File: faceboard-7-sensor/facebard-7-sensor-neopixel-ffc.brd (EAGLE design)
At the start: 27 x 93.4 mm, 33 parts, among them J1 686114148922, J2 686114148922, Q1 QRE1113, Q2 QRE1113, Q3 QRE1113, Q4 QRE1113, Q5 QRE1113, Q6 QRE1113, Q7 QRE1113, U1 CD4051BE

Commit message: add ffc
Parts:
- removed J2: 686114148922, 686114148922:686114148922
- added FFCIN, FFCOUT: 52806-1410, 52806-1410:528061410
- added J3: 1-1734592-4, 1-1734592-4:CONN_1-1734592-4_TYCO
- added SJ1, SJ2, SJ3, SJ4, SJ5, SJ6, SJ7: (no value), jumper:SJ
- J1: value 686114148922 -> 1-1734592-4; device 686114148922:686114148922 -> 1-1734592-4:CONN_1-1734592-4_TYCO
- moved J1 8.14 mm to (18.0, 86.0), turned to 0 degrees
- moved D1 2.08 mm to (25.9, 2.61)
- moved D2 2.08 mm to (25.9, 16.6)
- moved D3 2.08 mm to (25.9, 30.6)
- moved D4 2.08 mm to (25.9, 44.7)
- moved D5 2.08 mm to (25.9, 58.7)
- moved D6 2.08 mm to (25.9, 72.7)
- moved D7 2.08 mm to (25.9, 86.7)
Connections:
- net 3V: now also FFCIN.2, FFCOUT.13, J1.2, J3.13; no longer J1.13, J2.2
- net 5V: now also FFCIN.3, FFCOUT.12, J1.3, J3.12; no longer J1.12, J2.3
- net A: now also FFCIN.4, FFCOUT.11, J1.4, J3.11; no longer J1.11, J2.4
- net B: now also FFCIN.5, FFCOUT.10, J1.5, J3.10; no longer J1.10, J2.5
- net C: now also FFCIN.6, FFCOUT.9, J1.6, J3.9; no longer J1.9, J2.6
- net GND: now also FFCIN.1, FFCOUT.14, J1.1, J3.14; no longer J1.14, J1.MP1, J1.MP2, J2.1, J2.MP1, J2.MP2
- net LEDDIN: now also FFCIN.7, J1.7; no longer J2.7
- net LEDDOUT: now also FFCOUT.8, J3.8; no longer J1.8
- net N$18: no longer D3.4
- net SIG: now also SJ1.2, SJ2.2, SJ3.2, SJ4.2, SJ5.2, SJ6.2, SJ7.2
- net SIG1: now also FFCIN.8, FFCOUT.7, J1.14, J3.1, SJ1.1; no longer J1.1, J2.14
- net SIG2: now also FFCIN.9, FFCOUT.6, J1.13, J3.2, SJ2.1; no longer J1.2, J2.13
- net SIG3: now also FFCIN.10, FFCOUT.5, J1.12, J3.3, SJ3.1; no longer J1.3, J2.12
- net SIG4: now also FFCIN.11, FFCOUT.4, J1.11, J3.4, SJ4.1; no longer J1.4, J2.11
- net SIG5: now also FFCIN.12, FFCOUT.3, J1.10, J3.5, SJ5.1; no longer J1.5, J2.10
- net SIG6: now also FFCIN.13, FFCOUT.2, J1.9, J3.6, SJ6.1; no longer J1.6, J2.9
- net SIG7: now also FFCIN.14, FFCOUT.1, J1.8, J3.7, SJ7.1; no longer J1.7, J2.8
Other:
- board size 27 x 93.4 mm -> 29 x 93.4 mm

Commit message: remove 0.5mm ffc
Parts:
- removed J1, J3: 1-1734592-4, 1-1734592-4:CONN_1-1734592-4_TYCO
- removed SV1, SV4: (no value), con-lstb:MA07-1
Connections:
- net 3V: no longer J1.2, J3.13
- net 5V: no longer J1.3, J3.12
- net A: no longer J1.4, J3.11
- net B: no longer J1.5, J3.10
- net C: no longer J1.6, J3.9
- net GND: no longer J1.1, J3.14
- net LEDDIN: no longer J1.7
- net LEDDOUT: no longer J3.8
- net N$18: now also D3.4
- net SIG: no longer SV1.1, SV1.2, SV1.3, SV1.4, SV1.5, SV1.6, SV1.7
- net SIG1: no longer J1.14, J3.1, SV4.1
- net SIG2: no longer J1.13, J3.2, SV4.2
- net SIG3: no longer J1.12, J3.3, SV4.3
- net SIG4: no longer J1.11, J3.4, SV4.4
- net SIG5: no longer J1.10, J3.5, SV4.5
- net SIG6: no longer J1.9, J3.6, SV4.6
- net SIG7: no longer J1.8, J3.7, SV4.7

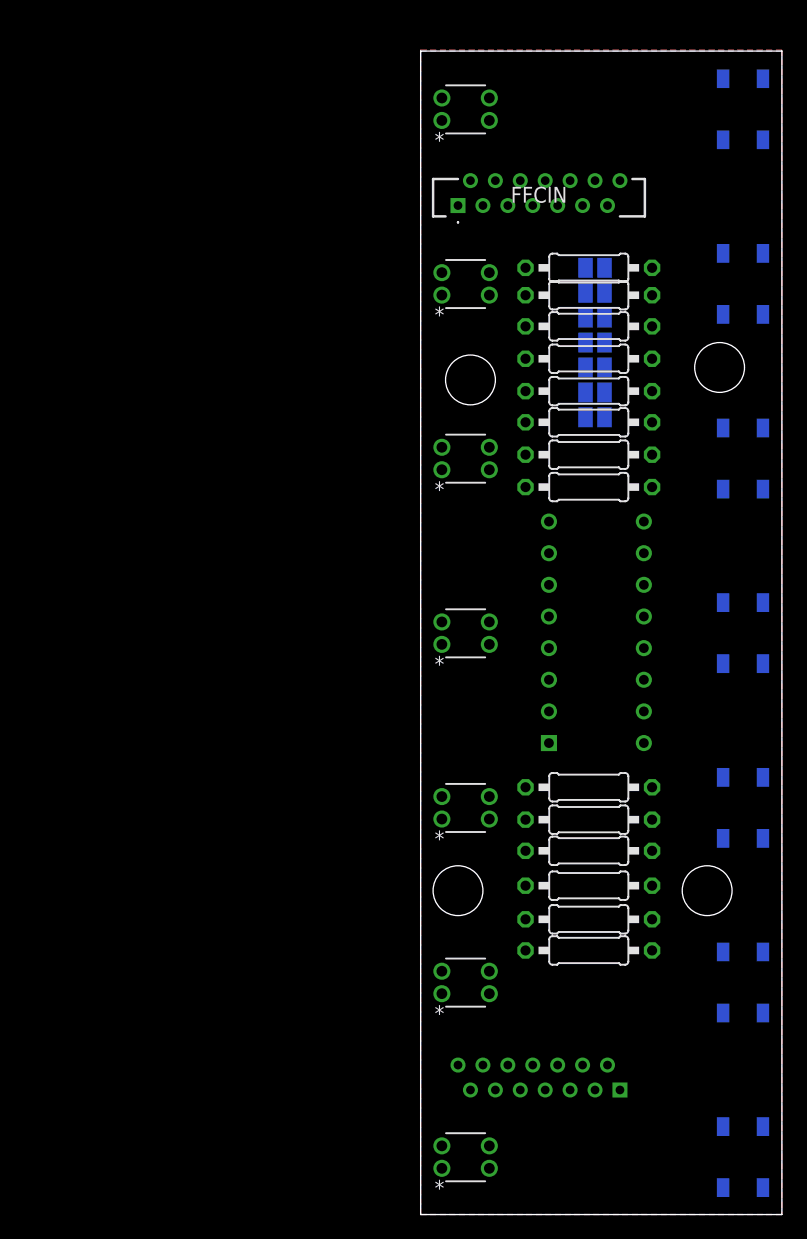
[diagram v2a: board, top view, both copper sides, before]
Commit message: add ffc boards
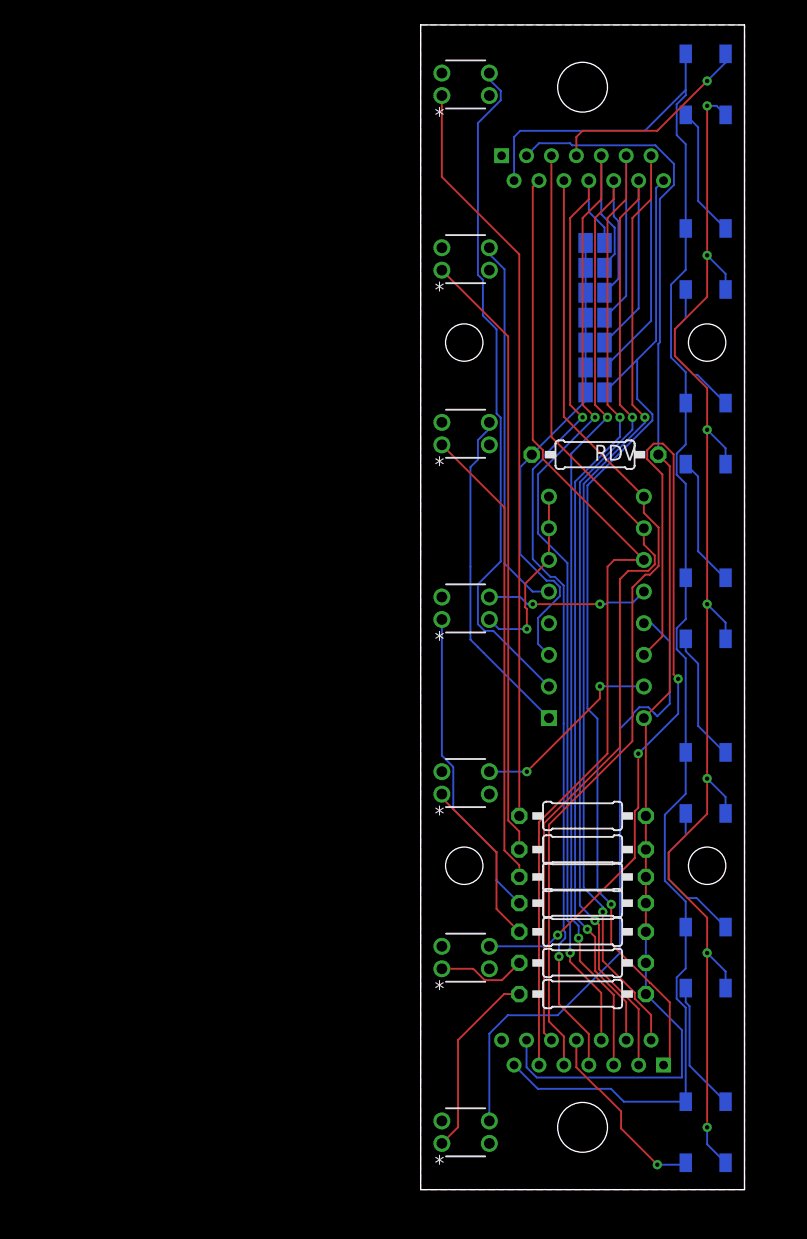
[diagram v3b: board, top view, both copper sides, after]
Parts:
- removed R10, R12, R14, R2, R4, R6, R8: 100k, rcl:0207/10
- added RDV: 1M, rcl:0207/10
- moved FFCOUT 75.6 mm to (6.50, 83.0), turned to 180 degrees
- moved FFCIN 70.9 mm to (19.5, 10.0), flipped to the bottom
- moved R13 44.0 mm to (13.0, 30.0)
- moved R11 42.0 mm to (13.0, 27.3)
- moved R9 39.0 mm to (13.0, 25.1)
- moved R7 36.0 mm to (13.0, 23.0)
- moved R3 9.01 mm to (13.0, 18.2)
- moved R5 9.01 mm to (13.0, 20.7)
- moved R1 6.02 mm to (13.0, 15.7)
- moved D1 3.61 mm to (22.9, 4.61)
- moved D2 3.61 mm to (22.9, 18.6)
- moved D3 3.61 mm to (22.9, 32.6)
- moved D4 3.61 mm to (22.9, 46.7)
- moved D5 3.61 mm to (22.9, 60.7)
- moved D6 3.61 mm to (22.9, 74.7)
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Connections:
- net 3V: now also FFCIN.13, FFCOUT.2; no longer FFCIN.2, FFCOUT.13
- net 5V: now also FFCIN.12, FFCOUT.3, RDV.2; no longer FFCIN.3, FFCOUT.12, R10.2, R12.2, R14.2, R2.2, R4.2, R6.2, R8.2
- net A: now also FFCIN.11, FFCOUT.4; no longer FFCIN.4, FFCOUT.11
- net B: now also FFCIN.10, FFCOUT.5; no longer FFCIN.5, FFCOUT.10
- net C: now also FFCIN.9, FFCOUT.6; no longer FFCIN.6, FFCOUT.9
- net GND: now also FFCIN.14, FFCOUT.1; no longer FFCIN.1, FFCOUT.14
- net LEDDIN: now also FFCIN.8; no longer FFCIN.7
- net LEDDOUT: now also FFCOUT.7; no longer FFCOUT.8
- net Q1SIG: no longer R2.1
- net Q2SIG: no longer R4.1
- net Q3SIG: no longer R6.1
- net Q4SIG: no longer R8.1
- net Q5SIG: no longer R10.1
- net Q6SIG: no longer R12.1
- net Q7SIG: no longer R14.1
- net SIG: now also RDV.1
- net SIG1: now also FFCIN.7, FFCOUT.8; no longer FFCIN.8, FFCOUT.7
- net SIG2: now also FFCIN.6, FFCOUT.9; no longer FFCIN.9, FFCOUT.6
- net SIG3: now also FFCIN.5, FFCOUT.10; no longer FFCIN.10, FFCOUT.5
- net SIG4: now also FFCIN.4, FFCOUT.11; no longer FFCIN.11, FFCOUT.4
- net SIG5: now also FFCIN.3, FFCOUT.12; no longer FFCIN.12, FFCOUT.3
- net SIG6: now also FFCIN.2, FFCOUT.13; no longer FFCIN.13, FFCOUT.2
- net SIG7: now also FFCIN.1, FFCOUT.14; no longer FFCIN.14, FFCOUT.1
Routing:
- net GND: track 0.00 -> 123.7 mm, vias 0 -> 8
- net 3V: track 0.00 -> 122.7 mm
- net 5V: track 0.00 -> 104.3 mm
- net SIG6: track 0.00 -> 94.9 mm, vias 0 -> 2
- net SIG5: track 0.00 -> 89.9 mm, vias 0 -> 2
- net SIG4: track 0.00 -> 88.9 mm, vias 0 -> 2
- net SIG2: track 0.00 -> 85.8 mm, vias 0 -> 2
- net SIG3: track 0.00 -> 84.3 mm, vias 0 -> 2
- net SIG1: track 0.00 -> 81.7 mm, vias 0 -> 2
- net SIG7: track 0.00 -> 81.2 mm, vias 0 -> 1
- net A: track 0.00 -> 79.8 mm
- net B: track 0.00 -> 79.4 mm
- net C: track 0.00 -> 78.5 mm
- net Q2SIG: track 0.00 -> 68.9 mm, vias 0 -> 3
- net N$13: track 0.00 -> 60.4 mm
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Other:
- board size 29 x 93.4 mm -> 26 x 93.5 mm
- board text added: "1"
- board text added: "2"
- board text added: "3"
- board text added: "4"
- board text added: "5"
- board text added: "6"
- board text added: "7"
- board text added: "NEMUS Face Board v0.1.1"
- board text removed: "3V"
- board text removed: "5V"
- board text removed: "A"
- board text removed: "C"
- board text removed: "DI"
- board text removed: "DO"
- board text removed: "GND"
- board text removed: "INT"
- board text removed: "NEMUS Face Board v0.1.0"
- board text removed: "SIG"

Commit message: tidy routing
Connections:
- net Q1SIG renamed C0
- net Q2SIG renamed C1
- net Q3SIG renamed C2
- net Q4SIG renamed C3
- net Q5SIG renamed C4
- net Q6SIG renamed C5
- net Q7SIG renamed C6
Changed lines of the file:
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@@
 <wire x1="6.7" y1="15.7" x2="7.92" y2="15.7" width="0.1524" layer="1"/>
 </signal>
-<signal name="Q1SIG">
+<signal name="C0">
 <contactref element="U1" pad="13"/>
-<contactref element="Q1" pad="3"/>
-<wire x1="5.515" y1="5.5134" x2="5.515" y2="12.515" width="0.1524" layer="16"/>
 <wire x1="5.515" y1="12.515" x2="7" y2="14" width="0.1524" layer="16"/>
 <wire x1="7" y1="14" x2="11" y2="14" width="0.1524" layer="16"/>
@@
 <wire x1="20" y1="39" x2="20" y2="44" width="0.1524" layer="16"/>
 <wire x1="20" y1="44" x2="18.53" y2="45.47" width="0.1524" layer="16"/>
+<contactref element="Q1" pad="3"/>
+<wire x1="5.515" y1="5.5134" x2="5.515" y2="12.515" width="0.1524" layer="16"/>
 </signal>
 <signal name="GND">
@@
 <wire x1="6.5356" y1="16.8156" x2="7.92" y2="18.2" width="0.1524" layer="1"/>
 </signal>
-<signal name="Q2SIG">
-<contactref element="Q2" pad="3"/>
+<signal name="C1">
 <contactref element="U1" pad="14"/>
 <via x="11" y="20.4334" extent="1-16" drill="0.35"/>
@@
 <wire x1="20.3048" y1="41.3684" x2="20.3048" y2="59.0324375" width="0.1524" layer="1"/>
 <wire x1="20.3048" y1="59.0324375" x2="19.4482375" y2="59.889" width="0.1524" layer="1"/>
+<wire x1="10.1" y1="19.5334" x2="11" y2="20.4334" width="0.1524" layer="16"/>
+<contactref element="Q2" pad="3"/>
 <wire x1="5.515" y1="19.5334" x2="10.1" y2="19.5334" width="0.1524" layer="16"/>
-<wire x1="10.1" y1="19.5334" x2="11" y2="20.4334" width="0.1524" layer="16"/>
 </signal>
 <signal name="N$5">
@@
 <wire x1="6.0922" y1="27.073725" x2="1.705" y2="31.460925" width="0.1524" layer="1"/>
 </signal>
-<signal name="Q3SIG">
-<contactref element="Q3" pad="3"/>
+<signal name="C2">
 <contactref element="U1" pad="15"/>
-<wire x1="5.515" y1="33.5534" x2="8.5268" y2="33.5534" width="0.1524" layer="16"/>
 <via x="8.5268" y="33.5534" extent="1-16" drill="0.35"/>
 <wire x1="8.5268" y1="33.5534" x2="14.3932" y2="39.4198" width="0.1524" layer="1"/>
@@
 <wire x1="14.3932" y1="40.4" x2="17.91" y2="40.4" width="0.1524" layer="16"/>
 <wire x1="17.91" y1="40.4" x2="17.92" y2="40.39" width="0.1524" layer="16"/>
+<contactref element="Q3" pad="3"/>
+<wire x1="5.515" y1="33.5534" x2="8.5268" y2="33.5534" width="0.1524" layer="16"/>
 </signal>
 <signal name="N$7">
@@
 <wire x1="2.6194" y1="30.546525" x2="2.6194" y2="33.9321625" width="0.1524" layer="16"/>
 </signal>
-<signal name="Q4SIG">
-<contactref element="Q4" pad="3"/>
+<signal name="C3">
 <contactref element="U1" pad="12"/>
-<wire x1="5.515" y1="47.5734" x2="8" y2="47.5734" width="0.1524" layer="16"/>
 <wire x1="15" y1="47.1337" x2="17.0437" y2="47.1337" width="0.1524" layer="16"/>
 <wire x1="17.0437" y1="47.1337" x2="17.92" y2="48.01" width="0.1524" layer="16"/>
-<wire x1="8" y1="47.5734" x2="8.5734" y2="47" width="0.1524" layer="16"/>
+<wire x1="8.0267" y1="47.5467" x2="8.5734" y2="47" width="0.1524" layer="16"/>
 <wire x1="8.5734" y1="47" x2="9" y2="47" width="0.1524" layer="16"/>
 <via x="9" y="47" extent="1-16" drill="0.35"/>
@@
 <wire x1="15" y1="47.1337" x2="14.8663" y2="47" width="0.1524" layer="16"/>
 <wire x1="9" y1="47" x2="14.3932" y2="47" width="0.1524" layer="1"/>
+<contactref element="Q4" pad="3"/>
+<wire x1="5.515" y1="47.5734" x2="8" y2="47.5734" width="0.1524" layer="16"/>
+<wire x1="8" y1="47.5734" x2="8.0267" y2="47.5467" width="0.1524" layer="16"/>
 </signal>
 <signal name="N$9">
@@
 <wire x1="6.7262" y1="27.2365625" x2="6.7262" y2="54.7688" width="0.1524" layer="1"/>
 </signal>
-<signal name="Q5SIG">
-<contactref element="Q5" pad="3"/>
+<signal name="C4">
 <contactref element="U1" pad="1"/>
-<wire x1="4.6006" y1="43.5494" x2="5.075" y2="43.075" width="0.1524" layer="16"/>
-<wire x1="5.075" y1="43.075" x2="10.3" y2="37.85" width="0.1524" layer="16"/>
-<wire x1="5.515" y1="61.5934" x2="5.515" y2="61.0831625" width="0.1524" layer="16"/>
+<wire x1="4" y1="44.15" x2="10.3" y2="37.85" width="0.1524" layer="16"/>
 <wire x1="4.6006" y1="58.6006" x2="4" y2="58" width="0.1524" layer="16"/>
 <wire x1="5.515" y1="61.0831625" x2="4.6006" y2="60.1687625" width="0.1524" layer="16"/>
 <wire x1="4.6006" y1="60.1687625" x2="4.6006" y2="58.6006" width="0.1524" layer="16"/>
-<wire x1="4" y1="58" x2="4" y2="50" width="0.1524" layer="16"/>
-<wire x1="4" y1="50" x2="4" y2="44.15" width="0.1524" layer="16"/>
-<wire x1="4" y1="44.15" x2="4.6006" y2="43.5494" width="0.1524" layer="16"/>
+<wire x1="4" y1="58" x2="4" y2="44.15" width="0.1524" layer="16"/>
+<contactref element="Q5" pad="3"/>
+<wire x1="5.515" y1="61.5934" x2="5.515" y2="61.0831625" width="0.1524" layer="16"/>
 </signal>
 <signal name="N$11">
@@
 <wire x1="7.031" y1="29.6317625" x2="7.031" y2="68.484" width="0.1524" layer="1"/>
 </signal>
-<signal name="Q6SIG">
-<contactref element="Q6" pad="3"/>
+<signal name="C5">
 <contactref element="U1" pad="5"/>
-<wire x1="5.515" y1="75.6134" x2="5.515" y2="75.1031625" width="0.1524" layer="16"/>
 <wire x1="5.515" y1="75.1031625" x2="6.7342" y2="73.8839625" width="0.1524" layer="16"/>
 <wire x1="6.7342" y1="73.8839625" x2="6.7342" y2="50.2658" width="0.1524" layer="16"/>
 <wire x1="8.99" y1="48.01" x2="10.3" y2="48.01" width="0.1524" layer="16"/>
 <wire x1="6.7342" y1="50.2658" x2="8.99" y2="48.01" width="0.1524" layer="16"/>
+<contactref element="Q6" pad="3"/>
+<wire x1="5.515" y1="75.6134" x2="5.515" y2="75.1031625" width="0.1524" layer="16"/>
 </signal>
 <signal name="N$13">
@@
 <wire x1="7.92" y1="75.08" x2="1.705" y2="81.295" width="0.1524" layer="1"/>
 </signal>
-<signal name="Q7SIG">
-<contactref element="Q7" pad="3"/>
+<signal name="C6">
 <contactref element="U1" pad="2"/>
 <wire x1="6.4294" y1="88.2087625" x2="6.4294" y2="87.4512375" width="0.1524" layer="16"/>
-<wire x1="5.515" y1="89.6334" x2="5.515" y2="89.1231625" width="0.1524" layer="16"/>
 <wire x1="5.515" y1="89.1231625" x2="6.4294" y2="88.2087625" width="0.1524" layer="16"/>
 <wire x1="4.6006" y1="73.4312375" x2="5" y2="73.0318375" width="0.1524" layer="16"/>
@@
 <wire x1="4.6006" y1="48.6006" x2="4.6006" y2="45.3912375" width="0.1524" layer="16"/>
 <wire x1="6.4294" y1="50.4294" x2="4.6006" y2="48.6006" width="0.1524" layer="16"/>
+<contactref element="Q7" pad="3"/>
+<wire x1="5.515" y1="89.6334" x2="5.515" y2="89.1231625" width="0.1524" layer="16"/>
 </signal>
 <signal name="SIG">

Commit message: change divide resistor value
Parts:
- RDV: value 1M -> 100k
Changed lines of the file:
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@@
 <attribute name="VALUE" x="13.5999" y="64" size="0.02" layer="28" rot="MR0"/>
 </element>
-<element name="RDV" library="rcl" library_urn="urn:adsk.eagle:library:334" package="0207/10" package3d_urn="urn:adsk.eagle:package:23491/2" value="1M" x="14" y="59" smashed="yes">
+<element name="RDV" library="rcl" library_urn="urn:adsk.eagle:library:334" package="0207/10" package3d_urn="urn:adsk.eagle:package:23491/2" value="100k" x="14" y="59" smashed="yes">
 <attribute name="NAME" x="13.952" y="58.524" size="1.27" layer="25" ratio="10"/>
 <attribute name="POPULARITY" value="81" x="14" y="59" size="1.778" layer="27" display="off"/>

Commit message: re-draw schematics
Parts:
- moved U1 44.4 mm to (-31.1, 21.9), flipped to the top, turned to 0 degrees
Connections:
- net LEDDIN renamed DIN
- net LEDDOUT renamed DOUT
- net SIG1 renamed S1
- net SIG2 renamed S2
- net SIG3 renamed S3
- net SIG4 renamed S4
- net SIG5 renamed S5
- net SIG6 renamed S6
- net SIG7 renamed S7
- removed net 5V: FFCIN.12, FFCOUT.3, R1.1, R11.1, R13.1, R3.1, R5.1, R7.1, R9.1, RDV.2, U1.16
- removed net N$9: Q5.1, R9.2
- new net N$2: FFCOUT.3, R1.1, R11.1, R13.1, R3.1, R5.1, R7.1, R9.1
- new net VCC: FFCIN.12, RDV.2, U1.16
- net GND: no longer FFCIN.14
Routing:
- net 5V: track 104.3 -> 0.00 mm
- net VCC: track 0.00 -> 38.2 mm
- net N$9: track 37.3 -> 0.00 mm
- net GND: track 123.7 -> 108.9 mm, vias 8 -> 7
- net A: track 79.8 -> 65.9 mm
- net C: track 78.5 -> 68.1 mm
- net C4: track 27.0 -> 18.1 mm
- net C6: track 54.7 -> 48.3 mm
- net S3: track 84.3 -> 78.6 mm
- net S6: track 94.9 -> 89.6 mm
- net S5: track 89.9 -> 85.4 mm
- net S1: track 81.7 -> 79.2 mm
- net C1: track 68.9 -> 66.8 mm
- net SIG: track 38.0 -> 36.0 mm
- net C5: track 30.4 -> 29.0 mm
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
